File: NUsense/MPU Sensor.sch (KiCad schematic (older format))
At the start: 4 parts, among them U9? MPU6000

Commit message: Add files
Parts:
- removed 0.1uF: C, symbol C
- added C?: 0.1uF, symbol C
- added R, R?: 2K, symbol R
- C: renamed from 0.1uF; value C -> 0.1uF
- C: renamed from 2.2nF; value C -> 2.2nF
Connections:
- net GND: now also C?.2
- net MPU_SCL: now also R.1
- net MPU_SDA/SDI: now also R?.2
- net at U9?.10 (REGOUT): now also C?.1
- net VDD5o5V renamed +3V3
- net +3V3: now also R.2, R?.1
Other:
- moved on the sheet: C
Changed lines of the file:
@@
 LIBS:valves
 LIBS:ADM6713RAKS
+LIBS:Header_Connectors
 LIBS:MPU6000
 LIBS:NUbots
 LIBS:STM32F746ZGT6
-LIBS:Header_Connectors
 LIBS:NUsense-cache
 EELAYER 25 0
@@
 L GND #PWR?
 U 1 1 5A698AEC
-P 4650 3800
-F 0 "#PWR?" H 4650 3550 50  0001 C CNN
-F 1 "GND" H 4650 3650 50  0000 C CNN
-F 2 "" H 4650 3800 50  0001 C CNN
-F 3 "" H 4650 3800 50  0001 C CNN
-	1    4650 3800
+P 4600 3800
+F 0 "#PWR?" H 4600 3550 50  0001 C CNN
+F 1 "GND" H 4600 3650 50  0000 C CNN
+F 2 "" H 4600 3800 50  0001 C CNN
+F 3 "" H 4600 3800 50  0001 C CNN
+	1    4600 3800
 	1    0    0    -1
 $EndComp
@@
 Wire Wire Line
 	6250 2850 6850 2850
-Text GLabel 6750 2100 1    60   Input ~ 0
-VDD5o5V
-$Comp
-L C 0.1uF
+$Comp
+L C C
 U 1 1 5A6D29D1
 P 7000 2850
-F 0 "0.1uF" H 7025 2950 50  0000 L CNN
-F 1 "C" H 7025 2750 50  0000 L CNN
+F 0 "C" H 7025 2950 50  0000 L CNN
+F 1 "0.1uF" H 7025 2750 50  0000 L CNN
 F 2 "" H 7038 2700 50  0001 C CNN
 F 3 "" H 7000 2850 50  0001 C CNN
@@
 	1    0    0    -1
 $EndComp
-$Comp
-L C 0.1uF
-U 1 1 5A6D2B51
-P 6850 3650
-F 0 "0.1uF" H 6875 3750 50  0000 L CNN
-F 1 "C" H 6875 3550 50  0000 L CNN
-F 2 "" H 6888 3500 50  0001 C CNN
-F 3 "" H 6850 3650 50  0001 C CNN
-	1    6850 3650
-	1    0    0    -1
-$EndComp
 Wire Wire Line
 	6850 3450 6850 3500
@@
 	6850 3800 6850 3850
 $Comp
-L C 2.2nF
+L C C
 U 1 1 5A6D2BCA
-P 4650 3400
-F 0 "2.2nF" H 4675 3500 50  0000 L CNN
-F 1 "C" H 4675 3300 50  0000 L CNN
-F 2 "" H 4688 3250 50  0001 C CNN
-F 3 "" H 4650 3400 50  0001 C CNN
-	1    4650 3400
-	1    0    0    -1
-$EndComp
-Wire Wire Line
-	5000 2450 4650 2450
-Wire Wire Line
-	4200 2850 5000 2850
-Wire Wire Line
-	4200 2750 5000 2750
+P 4600 3400
+F 0 "C" H 4625 3500 50  0000 L CNN
+F 1 "2.2nF" H 4625 3300 50  0000 L CNN
+F 2 "" H 4638 3250 50  0001 C CNN
+F 3 "" H 4600 3400 50  0001 C CNN
+	1    4600 3400
+	1    0    0    -1
+$EndComp
+Wire Wire Line
+	4600 2450 5000 2450
 Wire Wire Line
 	6250 3250 7750 3250
@@
 Wire Wire Line
 	7150 3350 7150 3500
-Text GLabel 7750 3250 2    60   Input ~ 0
+Wire Wire Line
+	5000 3250 4850 3250
+Wire Wire Line
+	4850 3250 4850 3650
+Wire Wire Line
+	4850 3650 4600 3650
+Wire Wire Line
+	4600 3550 4600 3800
+Connection ~ 4600 3650
+Wire Wire Line
+	4600 2450 4600 3250
+$Comp
+L +3.3V #PWR?
+U 1 1 5A6FD48D
+P 6750 2100
+F 0 "#PWR?" H 6750 1950 50  0001 C CNN
+F 1 "+3.3V" H 6750 2240 50  0000 C CNN
+F 2 "" H 6750 2100 50  0001 C CNN
+F 3 "" H 6750 2100 50  0001 C CNN
+	1    6750 2100
+	1    0    0    -1
+$EndComp
+Wire Wire Line
+	4200 2850 5000 2850
+Wire Wire Line
+	5000 2750 4200 2750
+Text HLabel 4200 2750 0    60   Output ~ 0
+MPU_SCL
+Text HLabel 4200 2850 0    60   Output ~ 0
+MPU_SDA/SDI
+Text HLabel 7750 3250 2    60   Output ~ 0
 MPU_INT
-Text GLabel 4200 2850 0    60   Input ~ 0
-MPU_SDA/SDI
-Text GLabel 4200 2750 0    60   Input ~ 0
-MPU_SCL
-Wire Wire Line
-	5000 3250 4850 3250
-Wire Wire Line
-	4850 3250 4850 3650
-Wire Wire Line
-	4850 3650 4650 3650
-Wire Wire Line
-	4650 3550 4650 3800
-Connection ~ 4650 3650
-Wire Wire Line
-	4650 2450 4650 3250
+$Comp
+L R R
+U 1 1 5A700977
+P 4350 2200
+F 0 "R" V 4430 2200 50  0000 C CNN
+F 1 "2K" V 4350 2200 50  0000 C CNN
+F 2 "" V 4280 2200 50  0001 C CNN
+F 3 "" H 4350 2200 50  0001 C CNN
+	1    4350 2200
+	-1   0    0    1
+$EndComp
+Wire Wire Line
+	4350 2350 4350 2750
+Connection ~ 4350 2750
+Wire Wire Line
+	4500 2350 4500 2850
+Connection ~ 4500 2850
+Wire Wire Line
+	4500 1850 4500 2050
+Wire Wire Line
+	4500 1950 4350 1950
+Wire Wire Line
+	4350 1950 4350 2050
+Connection ~ 4500 1950
+$Comp
+L +3.3V #PWR?
+U 1 1 5A700A52
+P 4500 1850
+F 0 "#PWR?" H 4500 1700 50  0001 C CNN
+F 1 "+3.3V" H 4500 1990 50  0000 C CNN
+F 2 "" H 4500 1850 50  0001 C CNN
+F 3 "" H 4500 1850 50  0001 C CNN
+	1    4500 1850
+	1    0    0    -1
+$EndComp
+$Comp
+L R R?
+U 1 1 5A704E41
+P 4500 2200
+F 0 "R?" V 4580 2200 50  0000 C CNN
+F 1 "2K" V 4500 2200 50  0000 C CNN
+F 2 "" V 4430 2200 50  0001 C CNN
+F 3 "" H 4500 2200 50  0001 C CNN
+	1    4500 2200
+	1    0    0    -1
+$EndComp
+$Comp
+L C C?
+U 1 1 5A704EA0
+P 6850 3650
+F 0 "C?" H 6875 3750 50  0000 L CNN
+F 1 "0.1uF" H 6875 3550 50  0000 L CNN
+F 2 "" H 6888 3500 50  0001 C CNN
+F 3 "" H 6850 3650 50  0001 C CNN
+	1    6850 3650
+	1    0    0    -1
+$EndComp
 $EndSCHEMATC

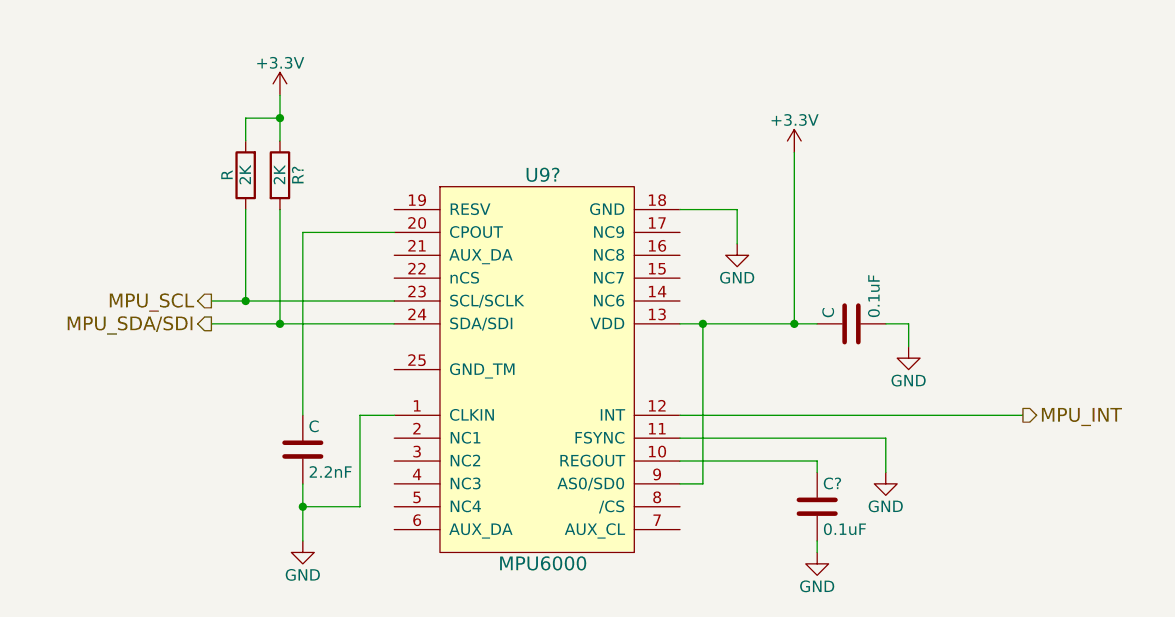
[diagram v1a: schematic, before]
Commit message: Adds annotations and footprints to all components
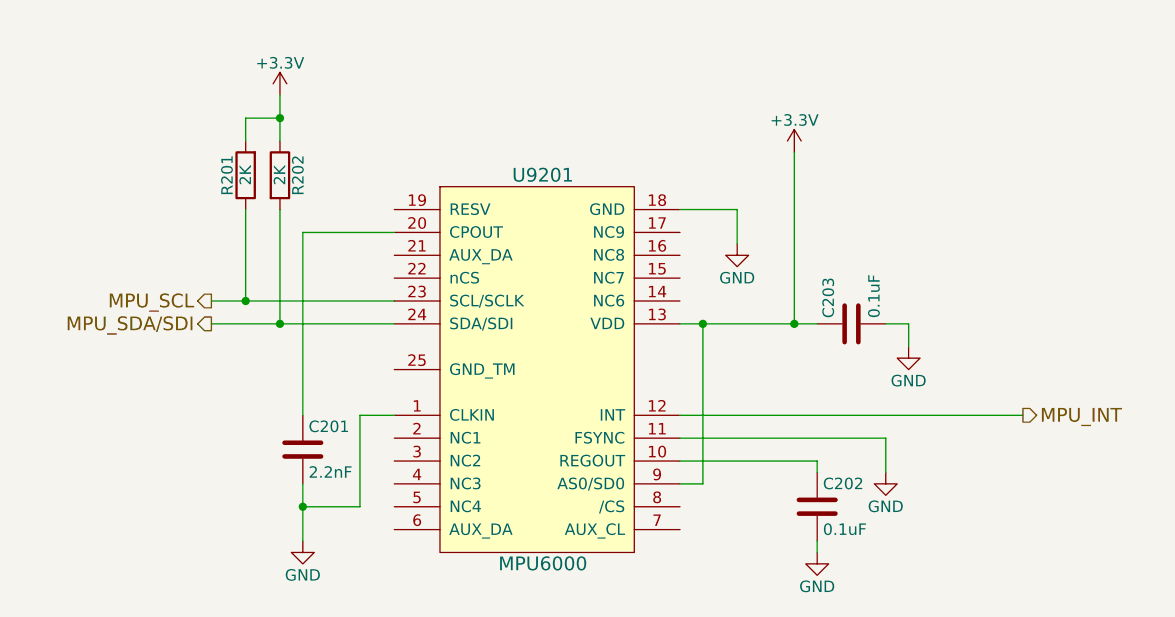
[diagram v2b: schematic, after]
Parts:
- C201, C203: renamed from C; footprint (none) -> Capacitors_SMD:C_0805_HandSoldering
- C202: renamed from C?; footprint (none) -> Capacitors_SMD:C_0805_HandSoldering
- R201: renamed from R; footprint (none) -> Resistors_SMD:R_0805_HandSoldering
- R202: renamed from R?; footprint (none) -> Resistors_SMD:R_0805_HandSoldering
- U9201: renamed from U9?; footprint (none) -> Footprints:QFP_24
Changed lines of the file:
@@
 $Descr A4 11693 8268
 encoding utf-8
-Sheet 2 9
+Sheet 2 12
 Title ""
 Date ""
@@
 $EndDescr
 $Comp
-L MPU6000 U9?
+L MPU6000 U9201
 U 1 1 5A6989D1
 P 5200 3850
-F 0 "U9?" H 5650 5500 60  0000 C CNN
+F 0 "U9201" H 5650 5500 60  0000 C CNN
 F 1 "MPU6000" H 5650 3800 60  0000 C CNN
-F 2 "" H 5200 3650 60  0001 C CNN
+F 2 "Footprints:QFP_24" H 5200 3650 60  0001 C CNN
 F 3 "" H 5200 3650 60  0001 C CNN
 	1    5200 3850
@@
 $EndComp
 $Comp
-L GND #PWR?
+L GND #PWR203
 U 1 1 5A698A78
 P 6500 2500
-F 0 "#PWR?" H 6500 2250 50  0001 C CNN
+F 0 "#PWR203" H 6500 2250 50  0001 C CNN
 F 1 "GND" H 6500 2350 50  0000 C CNN
 F 2 "" H 6500 2500 50  0001 C CNN
@@
 $EndComp
 $Comp
-L GND #PWR?
+L GND #PWR202
 U 1 1 5A698AEC
 P 4600 3800
-F 0 "#PWR?" H 4600 3550 50  0001 C CNN
+F 0 "#PWR202" H 4600 3550 50  0001 C CNN
 F 1 "GND" H 4600 3650 50  0000 C CNN
 F 2 "" H 4600 3800 50  0001 C CNN
@@
 	6250 2850 6850 2850
 $Comp
-L C C
+L C C203
 U 1 1 5A6D29D1
 P 7000 2850
-F 0 "C" H 7025 2950 50  0000 L CNN
+F 0 "C203" H 7025 2950 50  0000 L CNN
 F 1 "0.1uF" H 7025 2750 50  0000 L CNN
-F 2 "" H 7038 2700 50  0001 C CNN
+F 2 "Capacitors_SMD:C_0805_HandSoldering" H 7038 2700 50  0001 C CNN
 F 3 "" H 7000 2850 50  0001 C CNN
 	1    7000 2850
@@
 	6750 2100 6750 2850
 $Comp
-L GND #PWR?
+L GND #PWR207
 U 1 1 5A6D2AC0
 P 7250 2950
-F 0 "#PWR?" H 7250 2700 50  0001 C CNN
+F 0 "#PWR207" H 7250 2700 50  0001 C CNN
 F 1 "GND" H 7250 2800 50  0000 C CNN
 F 2 "" H 7250 2950 50  0001 C CNN
@@
 	6500 2350 6500 2500
 $Comp
-L GND #PWR?
+L GND #PWR206
 U 1 1 5A6D2B2A
 P 7150 3500
-F 0 "#PWR?" H 7150 3250 50  0001 C CNN
+F 0 "#PWR206" H 7150 3250 50  0001 C CNN
 F 1 "GND" H 7150 3350 50  0000 C CNN
 F 2 "" H 7150 3500 50  0001 C CNN
@@
 	6850 3450 6850 3500
 $Comp
-L GND #PWR?
+L GND #PWR205
 U 1 1 5A6D2BA4
 P 6850 3850
-F 0 "#PWR?" H 6850 3600 50  0001 C CNN
+F 0 "#PWR205" H 6850 3600 50  0001 C CNN
 F 1 "GND" H 6850 3700 50  0000 C CNN
 F 2 "" H 6850 3850 50  0001 C CNN
@@
 	6850 3800 6850 3850
 $Comp
-L C C
+L C C201
 U 1 1 5A6D2BCA
 P 4600 3400
-F 0 "C" H 4625 3500 50  0000 L CNN
+F 0 "C201" H 4625 3500 50  0000 L CNN
 F 1 "2.2nF" H 4625 3300 50  0000 L CNN
-F 2 "" H 4638 3250 50  0001 C CNN
+F 2 "Capacitors_SMD:C_0805_HandSoldering" H 4638 3250 50  0001 C CNN
 F 3 "" H 4600 3400 50  0001 C CNN
 	1    4600 3400
@@
 	4600 2450 4600 3250
 $Comp
-L +3.3V #PWR?
+L +3.3V #PWR204
 U 1 1 5A6FD48D
 P 6750 2100
-F 0 "#PWR?" H 6750 1950 50  0001 C CNN
+F 0 "#PWR204" H 6750 1950 50  0001 C CNN
 F 1 "+3.3V" H 6750 2240 50  0000 C CNN
 F 2 "" H 6750 2100 50  0001 C CNN
@@
 MPU_INT
 $Comp
-L R R
+L R R201
 U 1 1 5A700977
 P 4350 2200
-F 0 "R" V 4430 2200 50  0000 C CNN
+F 0 "R201" V 4430 2200 50  0000 C CNN
 F 1 "2K" V 4350 2200 50  0000 C CNN
-F 2 "" V 4280 2200 50  0001 C CNN
+F 2 "Resistors_SMD:R_0805_HandSoldering" V 4280 2200 50  0001 C CNN
 F 3 "" H 4350 2200 50  0001 C CNN
 	1    4350 2200
@@
 Connection ~ 4500 1950
 $Comp
-L +3.3V #PWR?
+L +3.3V #PWR201
 U 1 1 5A700A52
 P 4500 1850
-F 0 "#PWR?" H 4500 1700 50  0001 C CNN
+F 0 "#PWR201" H 4500 1700 50  0001 C CNN
 F 1 "+3.3V" H 4500 1990 50  0000 C CNN
 F 2 "" H 4500 1850 50  0001 C CNN
@@
 $EndComp
 $Comp
-L R R?
+L R R202
 U 1 1 5A704E41
 P 4500 2200
-F 0 "R?" V 4580 2200 50  0000 C CNN
+F 0 "R202" V 4580 2200 50  0000 C CNN
 F 1 "2K" V 4500 2200 50  0000 C CNN
-F 2 "" V 4430 2200 50  0001 C CNN
+F 2 "Resistors_SMD:R_0805_HandSoldering" V 4430 2200 50  0001 C CNN
 F 3 "" H 4500 2200 50  0001 C CNN
 	1    4500 2200
@@
 $EndComp
 $Comp
-L C C?
+L C C202
 U 1 1 5A704EA0
 P 6850 3650
-F 0 "C?" H 6875 3750 50  0000 L CNN
+F 0 "C202" H 6875 3750 50  0000 L CNN
 F 1 "0.1uF" H 6875 3550 50  0000 L CNN
-F 2 "" H 6888 3500 50  0001 C CNN
+F 2 "Capacitors_SMD:C_0805_HandSoldering" H 6888 3500 50  0001 C CNN
 F 3 "" H 6850 3650 50  0001 C CNN
 	1    6850 3650

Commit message: More Changes
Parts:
- renumbered U9201 to U201
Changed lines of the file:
@@
 $EndDescr
 $Comp
-L MPU6000 U9201
+L MPU6000 U201
 U 1 1 5A6989D1
 P 5200 3850
-F 0 "U9201" H 5650 5500 60  0000 C CNN
+F 0 "U201" H 5650 5500 60  0000 C CNN
 F 1 "MPU6000" H 5650 3800 60  0000 C CNN
 F 2 "Footprints:QFP_24" H 5200 3650 60  0001 C CNN
@@
 $EndComp
 $Comp
-L GND #PWR203
+L GND #PWR02
 U 1 1 5A698A78
 P 6500 2500
-F 0 "#PWR203" H 6500 2250 50  0001 C CNN
+F 0 "#PWR02" H 6500 2250 50  0001 C CNN
 F 1 "GND" H 6500 2350 50  0000 C CNN
 F 2 "" H 6500 2500 50  0001 C CNN
@@
 $EndComp
 $Comp
-L GND #PWR202
+L GND #PWR03
 U 1 1 5A698AEC
 P 4600 3800
-F 0 "#PWR202" H 4600 3550 50  0001 C CNN
+F 0 "#PWR03" H 4600 3550 50  0001 C CNN
 F 1 "GND" H 4600 3650 50  0000 C CNN
 F 2 "" H 4600 3800 50  0001 C CNN
@@
 	6750 2100 6750 2850
 $Comp
-L GND #PWR207
+L GND #PWR04
 U 1 1 5A6D2AC0
 P 7250 2950
-F 0 "#PWR207" H 7250 2700 50  0001 C CNN
+F 0 "#PWR04" H 7250 2700 50  0001 C CNN
 F 1 "GND" H 7250 2800 50  0000 C CNN
 F 2 "" H 7250 2950 50  0001 C CNN
@@
 	6500 2350 6500 2500
 $Comp
-L GND #PWR206
+L GND #PWR05
 U 1 1 5A6D2B2A
 P 7150 3500
-F 0 "#PWR206" H 7150 3250 50  0001 C CNN
+F 0 "#PWR05" H 7150 3250 50  0001 C CNN
 F 1 "GND" H 7150 3350 50  0000 C CNN
 F 2 "" H 7150 3500 50  0001 C CNN
@@
 	6850 3450 6850 3500
 $Comp
-L GND #PWR205
+L GND #PWR06
 U 1 1 5A6D2BA4
 P 6850 3850
-F 0 "#PWR205" H 6850 3600 50  0001 C CNN
+F 0 "#PWR06" H 6850 3600 50  0001 C CNN
 F 1 "GND" H 6850 3700 50  0000 C CNN
 F 2 "" H 6850 3850 50  0001 C CNN
@@
 	4600 2450 4600 3250
 $Comp
-L +3.3V #PWR204
+L +3.3V #PWR07
 U 1 1 5A6FD48D
 P 6750 2100
-F 0 "#PWR204" H 6750 1950 50  0001 C CNN
+F 0 "#PWR07" H 6750 1950 50  0001 C CNN
 F 1 "+3.3V" H 6750 2240 50  0000 C CNN
 F 2 "" H 6750 2100 50  0001 C CNN
@@
 Connection ~ 4500 1950
 $Comp
-L +3.3V #PWR201
+L +3.3V #PWR08
 U 1 1 5A700A52
 P 4500 1850
-F 0 "#PWR201" H 4500 1700 50  0001 C CNN
+F 0 "#PWR08" H 4500 1700 50  0001 C CNN
 F 1 "+3.3V" H 4500 1990 50  0000 C CNN
 F 2 "" H 4500 1850 50  0001 C CNN

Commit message: Cleans up some minor things
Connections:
- net +3V3: now also C203.2; no longer C203.1
- net GND: now also C203.1; no longer C203.2
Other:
- moved on the sheet: C203
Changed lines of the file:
@@
 $EndComp
 $Comp
-L GND #PWR4
+L GND #PWR203
 U 1 1 5A698A78
-P 6500 2500
-F 0 "#PWR4" H 6500 2250 50  0001 C CNN
-F 1 "GND" H 6500 2350 50  0000 C CNN
-F 2 "" H 6500 2500 50  0001 C CNN
-F 3 "" H 6500 2500 50  0001 C CNN
-	1    6500 2500
+P 6350 2400
+F 0 "#PWR203" H 6350 2150 50  0001 C CNN
+F 1 "GND" H 6350 2250 50  0000 C CNN
+F 2 "" H 6350 2400 50  0001 C CNN
+F 3 "" H 6350 2400 50  0001 C CNN
+	1    6350 2400
 	1    0    0    -1
 $EndComp
 $Comp
-L GND #PWR3
+L GND #PWR202
 U 1 1 5A698AEC
 P 4600 3800
-F 0 "#PWR3" H 4600 3550 50  0001 C CNN
+F 0 "#PWR202" H 4600 3550 50  0001 C CNN
 F 1 "GND" H 4600 3650 50  0000 C CNN
 F 2 "" H 4600 3800 50  0001 C CNN
@@
 	1    0    0    -1
 $EndComp
-Wire Wire Line
-	6250 2350 6500 2350
-Wire Wire Line
-	6250 2850 6850 2850
 $Comp
 L C C203
 U 1 1 5A6D29D1
-P 7000 2850
-F 0 "C203" H 7025 2950 50  0000 L CNN
-F 1 "0.1uF" H 7025 2750 50  0000 L CNN
-F 2 "Capacitors_SMD:C_0805_HandSoldering" H 7038 2700 50  0001 C CNN
-F 3 "" H 7000 2850 50  0001 C CNN
-	1    7000 2850
-	0    -1   -1   0
-$EndComp
-Connection ~ 6750 2850
-Wire Wire Line
-	6750 2100 6750 2850
-$Comp
-L GND #PWR8
-U 1 1 5A6D2AC0
-P 7250 2950
-F 0 "#PWR8" H 7250 2700 50  0001 C CNN
-F 1 "GND" H 7250 2800 50  0000 C CNN
-F 2 "" H 7250 2950 50  0001 C CNN
-F 3 "" H 7250 2950 50  0001 C CNN
-	1    7250 2950
+P 6600 2550
+F 0 "C203" H 6625 2650 50  0000 L CNN
+F 1 "0.1uF" H 6625 2450 50  0000 L CNN
+F 2 "Capacitors_SMD:C_0805_HandSoldering" H 6638 2400 50  0001 C CNN
+F 3 "" H 6600 2550 50  0001 C CNN
+	1    6600 2550
 	1    0    0    -1
 $EndComp
-Wire Wire Line
-	7150 2850 7250 2850
-Wire Wire Line
-	7250 2850 7250 2950
-Wire Wire Line
-	6500 2350 6500 2500
 $Comp
-L GND #PWR7
+L GND #PWR206
 U 1 1 5A6D2B2A
 P 7150 3500
-F 0 "#PWR7" H 7150 3250 50  0001 C CNN
+F 0 "#PWR206" H 7150 3250 50  0001 C CNN
 F 1 "GND" H 7150 3350 50  0000 C CNN
 F 2 "" H 7150 3500 50  0001 C CNN
@@
 	6850 3450 6850 3500
 $Comp
-L GND #PWR6
+L GND #PWR205
 U 1 1 5A6D2BA4
 P 6850 3850
-F 0 "#PWR6" H 6850 3600 50  0001 C CNN
+F 0 "#PWR205" H 6850 3600 50  0001 C CNN
 F 1 "GND" H 6850 3700 50  0000 C CNN
 F 2 "" H 6850 3850 50  0001 C CNN
@@
 	4600 2450 4600 3250
 $Comp
-L +3.3V #PWR5
+L +3.3V #PWR204
 U 1 1 5A6FD48D
-P 6750 2100
-F 0 "#PWR5" H 6750 1950 50  0001 C CNN
-F 1 "+3.3V" H 6750 2240 50  0000 C CNN
-F 2 "" H 6750 2100 50  0001 C CNN
-F 3 "" H 6750 2100 50  0001 C CNN
-	1    6750 2100
+P 6950 2800
+F 0 "#PWR204" H 6950 2650 50  0001 C CNN
+F 1 "+3.3V" H 6950 2940 50  0000 C CNN
+F 2 "" H 6950 2800 50  0001 C CNN
+F 3 "" H 6950 2800 50  0001 C CNN
+	1    6950 2800
 	1    0    0    -1
 $EndComp
@@
 Connection ~ 4500 1950
 $Comp
-L +3.3V #PWR2
+L +3.3V #PWR201
 U 1 1 5A700A52
 P 4500 1850
-F 0 "#PWR2" H 4500 1700 50  0001 C CNN
+F 0 "#PWR201" H 4500 1700 50  0001 C CNN
 F 1 "+3.3V" H 4500 1990 50  0000 C CNN
 F 2 "" H 4500 1850 50  0001 C CNN
@@
 	1    0    0    -1
 $EndComp
+Wire Wire Line
+	6250 2350 6600 2350
+Wire Wire Line
+	6350 2350 6350 2400
+Wire Wire Line
+	6600 2350 6600 2400
+Connection ~ 6350 2350
+Wire Wire Line
+	6600 2700 6600 2850
+Wire Wire Line
+	6250 2850 6950 2850
+Wire Wire Line
+	6950 2850 6950 2800
+Connection ~ 6600 2850
 $EndSCHEMATC

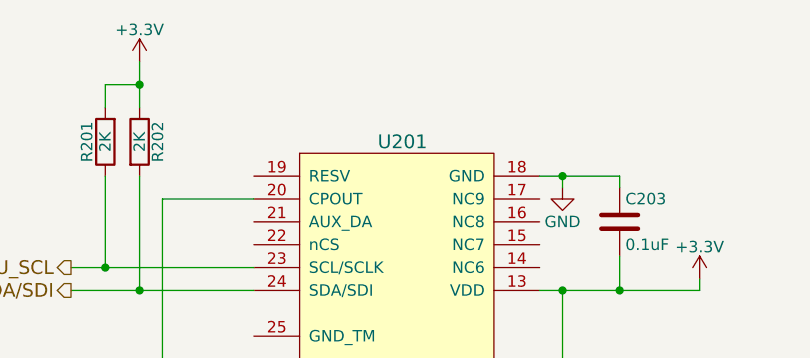
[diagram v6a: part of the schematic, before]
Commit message: Add labels
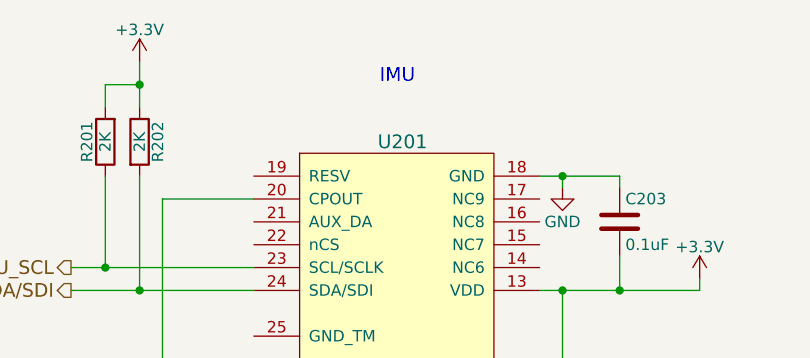
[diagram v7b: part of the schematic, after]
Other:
- note added: "IMU"
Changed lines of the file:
@@
 	6950 2850 6950 2800
 Connection ~ 6600 2850
+Text Notes 5550 1950 0    60   ~ 0
+IMU
 $EndSCHEMATC
